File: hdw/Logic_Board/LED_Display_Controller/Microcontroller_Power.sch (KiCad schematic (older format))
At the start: 31 parts, among them U601 PIC32MZ2048EFH144_IPL

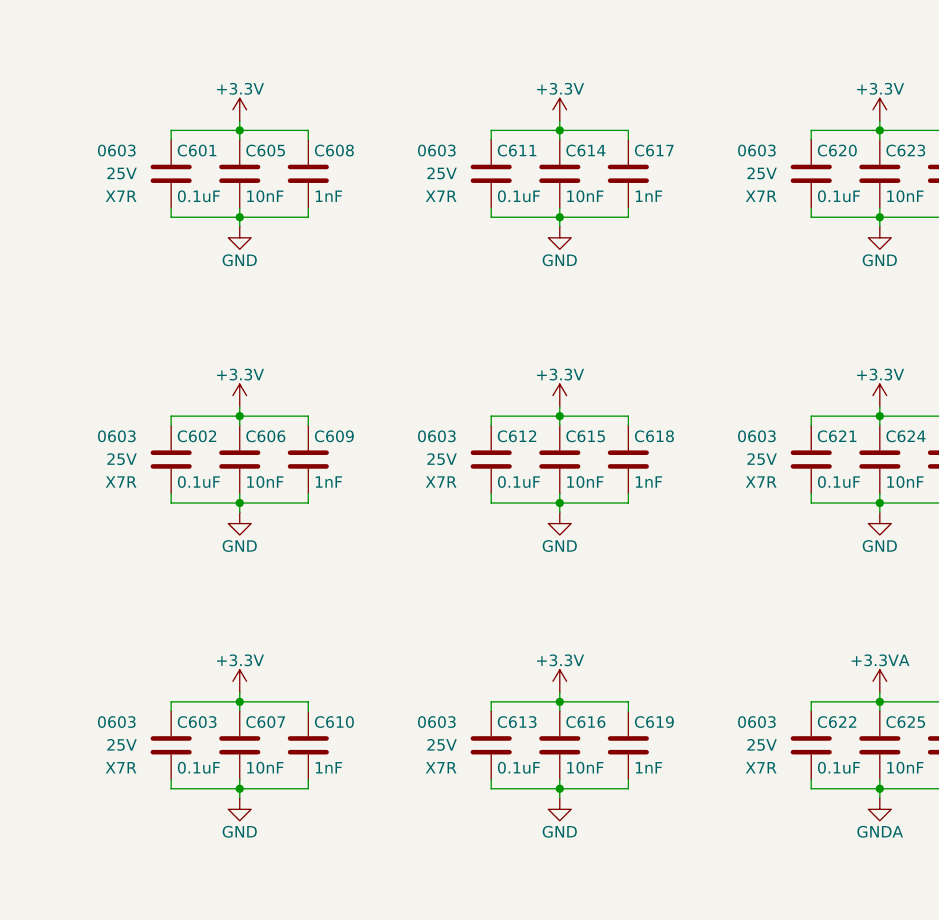
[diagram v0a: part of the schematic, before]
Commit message: Added some digikey partnumbers to components
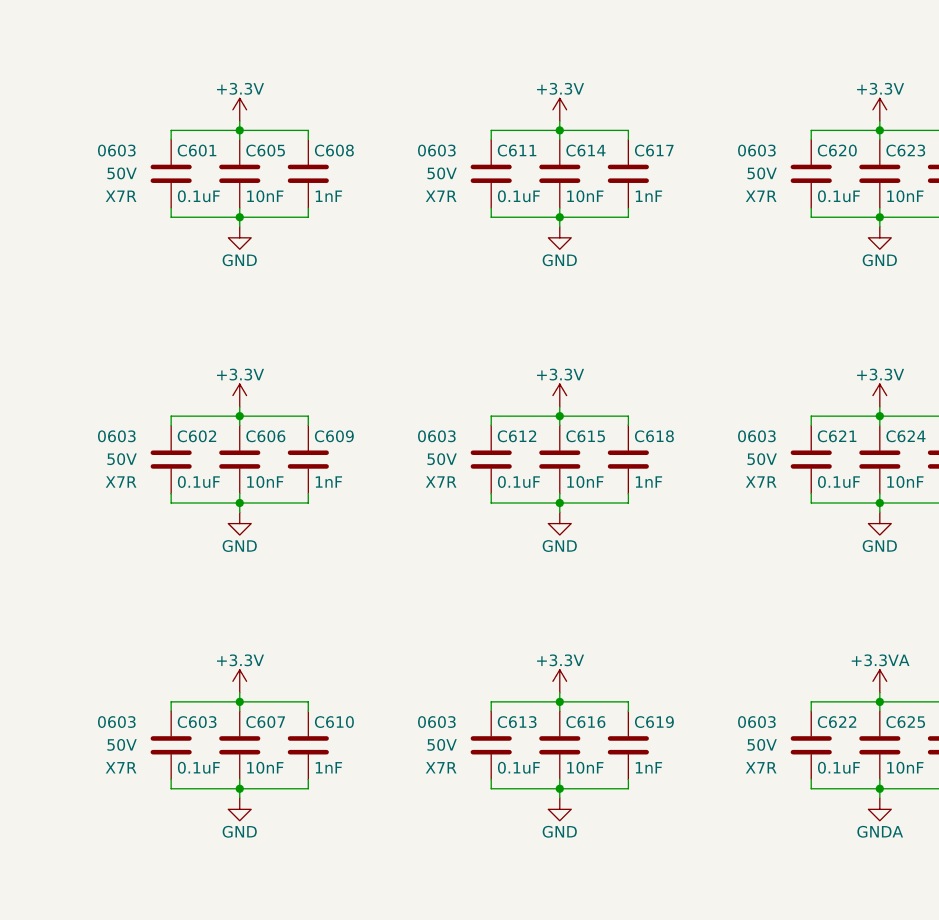
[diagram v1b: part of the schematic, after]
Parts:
- C601, C602, C603, C611, C612, C613, C620, C621, C622: footprint (none) -> Capacitors_SMD:C_0603; Digi-Key PN PN -> 311-1344-1-ND; Voltage 25V -> 50V
- C605, C606, C607, C614, C615, C616, C623, C624, C625: Digi-Key PN PN -> 1276-1921-1-ND; Voltage 25V -> 50V
- C608, C609, C610, C617, C618, C619, C626, C627, C628: Digi-Key PN PN -> 1276-1018-1-ND; Voltage 25V -> 50V
- L601, L602: Digi-Key PN (none) -> 732-2389-1-ND
- U601: Config ALL -> (none)

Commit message: First pass assignment of footprints to all components
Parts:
- C604: footprint (none) -> Capacitors_Tantalum_SMD:CP_Tantalum_Case-B_EIA-3528-21_Reflow
- C605, C606, C607, C608, C609, C610, C614, C615, C616, C617, C618, C619, C623, C624, C625, C626, C627, C628: footprint (none) -> Capacitors_SMD:C_0603
- L601, L602: footprint (none) -> Inductors_SMD:L_0603
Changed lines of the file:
@@
 F 0 "C605" H 1545 1750 50  0000 L CNN
 F 1 "10nF" H 1545 1550 50  0000 L CNN
-F 2 "" H 1558 1500 50  0001 C CNN
+F 2 "Capacitors_SMD:C_0603" H 1558 1500 50  0001 C CNN
 F 3 "" H 1545 1750 50  0001 C CNN
 F 4 "0603" H 1370 1750 50  0001 R CNN "display_footprint"
@@
 F 0 "C608" H 1845 1750 50  0000 L CNN
 F 1 "1nF" H 1845 1550 50  0000 L CNN
-F 2 "" H 1858 1500 50  0001 C CNN
+F 2 "Capacitors_SMD:C_0603" H 1858 1500 50  0001 C CNN
 F 3 "" H 1845 1750 50  0001 C CNN
 F 4 "0603" H 1670 1750 50  0001 R CNN "display_footprint"
@@
 F 0 "C614" H 2945 1750 50  0000 L CNN
 F 1 "10nF" H 2945 1550 50  0000 L CNN
-F 2 "" H 2958 1500 50  0001 C CNN
+F 2 "Capacitors_SMD:C_0603" H 2958 1500 50  0001 C CNN
 F 3 "" H 2945 1750 50  0001 C CNN
 F 4 "0603" H 2770 1750 50  0001 R CNN "display_footprint"
@@
 F 0 "C617" H 3245 1750 50  0000 L CNN
 F 1 "1nF" H 3245 1550 50  0000 L CNN
-F 2 "" H 3258 1500 50  0001 C CNN
+F 2 "Capacitors_SMD:C_0603" H 3258 1500 50  0001 C CNN
 F 3 "" H 3245 1750 50  0001 C CNN
 F 4 "0603" H 3070 1750 50  0001 R CNN "display_footprint"
@@
 F 0 "C623" H 4345 1750 50  0000 L CNN
 F 1 "10nF" H 4345 1550 50  0000 L CNN
-F 2 "" H 4358 1500 50  0001 C CNN
+F 2 "Capacitors_SMD:C_0603" H 4358 1500 50  0001 C CNN
 F 3 "" H 4345 1750 50  0001 C CNN
 F 4 "0603" H 4170 1750 50  0001 R CNN "display_footprint"
@@
 F 0 "C626" H 4645 1750 50  0000 L CNN
 F 1 "1nF" H 4645 1550 50  0000 L CNN
-F 2 "" H 4658 1500 50  0001 C CNN
+F 2 "Capacitors_SMD:C_0603" H 4658 1500 50  0001 C CNN
 F 3 "" H 4645 1750 50  0001 C CNN
 F 4 "0603" H 4470 1750 50  0001 R CNN "display_footprint"
@@
 F 0 "C606" H 1545 3000 50  0000 L CNN
 F 1 "10nF" H 1545 2800 50  0000 L CNN
-F 2 "" H 1558 2750 50  0001 C CNN
+F 2 "Capacitors_SMD:C_0603" H 1558 2750 50  0001 C CNN
 F 3 "" H 1545 3000 50  0001 C CNN
 F 4 "0603" H 1370 3000 50  0001 R CNN "display_footprint"
@@
 F 0 "C609" H 1845 3000 50  0000 L CNN
 F 1 "1nF" H 1845 2800 50  0000 L CNN
-F 2 "" H 1858 2750 50  0001 C CNN
+F 2 "Capacitors_SMD:C_0603" H 1858 2750 50  0001 C CNN
 F 3 "" H 1845 3000 50  0001 C CNN
 F 4 "0603" H 1670 3000 50  0001 R CNN "display_footprint"
@@
 F 0 "C615" H 2945 3000 50  0000 L CNN
 F 1 "10nF" H 2945 2800 50  0000 L CNN
-F 2 "" H 2958 2750 50  0001 C CNN
+F 2 "Capacitors_SMD:C_0603" H 2958 2750 50  0001 C CNN
 F 3 "" H 2945 3000 50  0001 C CNN
 F 4 "0603" H 2770 3000 50  0001 R CNN "display_footprint"
@@
 F 0 "C618" H 3245 3000 50  0000 L CNN
 F 1 "1nF" H 3245 2800 50  0000 L CNN
-F 2 "" H 3258 2750 50  0001 C CNN
+F 2 "Capacitors_SMD:C_0603" H 3258 2750 50  0001 C CNN
 F 3 "" H 3245 3000 50  0001 C CNN
 F 4 "0603" H 3070 3000 50  0001 R CNN "display_footprint"
@@
 F 0 "C624" H 4345 3000 50  0000 L CNN
 F 1 "10nF" H 4345 2800 50  0000 L CNN
-F 2 "" H 4358 2750 50  0001 C CNN
+F 2 "Capacitors_SMD:C_0603" H 4358 2750 50  0001 C CNN
 F 3 "" H 4345 3000 50  0001 C CNN
 F 4 "0603" H 4170 3000 50  0001 R CNN "display_footprint"
@@
 F 0 "C627" H 4645 3000 50  0000 L CNN
 F 1 "1nF" H 4645 2800 50  0000 L CNN
-F 2 "" H 4658 2750 50  0001 C CNN
+F 2 "Capacitors_SMD:C_0603" H 4658 2750 50  0001 C CNN
 F 3 "" H 4645 3000 50  0001 C CNN
 F 4 "0603" H 4470 3000 50  0001 R CNN "display_footprint"
@@
 F 0 "C607" H 1545 4250 50  0000 L CNN
 F 1 "10nF" H 1545 4050 50  0000 L CNN
-F 2 "" H 1558 4000 50  0001 C CNN
+F 2 "Capacitors_SMD:C_0603" H 1558 4000 50  0001 C CNN
 F 3 "" H 1545 4250 50  0001 C CNN
 F 4 "0603" H 1370 4250 50  0001 R CNN "display_footprint"
@@
 F 0 "C610" H 1845 4250 50  0000 L CNN
 F 1 "1nF" H 1845 4050 50  0000 L CNN
-F 2 "" H 1858 4000 50  0001 C CNN
+F 2 "Capacitors_SMD:C_0603" H 1858 4000 50  0001 C CNN
 F 3 "" H 1845 4250 50  0001 C CNN
 F 4 "0603" H 1670 4250 50  0001 R CNN "display_footprint"
@@
 F 0 "C616" H 2945 4250 50  0000 L CNN
 F 1 "10nF" H 2945 4050 50  0000 L CNN
-F 2 "" H 2958 4000 50  0001 C CNN
+F 2 "Capacitors_SMD:C_0603" H 2958 4000 50  0001 C CNN
 F 3 "" H 2945 4250 50  0001 C CNN
 F 4 "0603" H 2770 4250 50  0001 R CNN "display_footprint"
@@
 F 0 "C619" H 3245 4250 50  0000 L CNN
 F 1 "1nF" H 3245 4050 50  0000 L CNN
-F 2 "" H 3258 4000 50  0001 C CNN
+F 2 "Capacitors_SMD:C_0603" H 3258 4000 50  0001 C CNN
 F 3 "" H 3245 4250 50  0001 C CNN
 F 4 "0603" H 3070 4250 50  0001 R CNN "display_footprint"
@@
 F 0 "C625" H 4345 4250 50  0000 L CNN
 F 1 "10nF" H 4345 4050 50  0000 L CNN
-F 2 "" H 4358 4000 50  0001 C CNN
+F 2 "Capacitors_SMD:C_0603" H 4358 4000 50  0001 C CNN
 F 3 "" H 4345 4250 50  0001 C CNN
 F 4 "0603" H 4170 4250 50  0001 R CNN "display_footprint"
@@
 F 0 "C628" H 4645 4250 50  0000 L CNN
 F 1 "1nF" H 4645 4050 50  0000 L CNN
-F 2 "" H 4658 4000 50  0001 C CNN
+F 2 "Capacitors_SMD:C_0603" H 4658 4000 50  0001 C CNN
 F 3 "" H 4645 4250 50  0001 C CNN
 F 4 "0603" H 4470 4250 50  0001 R CNN "display_footprint"
@@
 F 0 "L601" V 2440 5815 50  0000 C CNN
 F 1 "600R 0.5A" V 2740 5790 50  0000 C CNN
-F 2 "" V 2520 5790 50  0001 C CNN
+F 2 "Inductors_SMD:L_0603" V 2520 5790 50  0001 C CNN
 F 3 "~" H 2590 5790 50  0001 C CNN
 F 4 "732-2389-1-ND" H 0   0   50  0001 C CNN "Digi-Key PN"
@@
 F 0 "L602" V 2440 6285 50  0000 C CNN
 F 1 "600R 0.5A" V 2740 6260 50  0000 C CNN
-F 2 "" V 2520 6260 50  0001 C CNN
+F 2 "Inductors_SMD:L_0603" V 2520 6260 50  0001 C CNN
 F 3 "~" H 2590 6260 50  0001 C CNN
 F 4 "732-2389-1-ND" H 0   0   50  0001 C CNN "Digi-Key PN"
@@
 F 0 "C604" H 1285 6080 50  0000 L CNN
 F 1 "100uF" H 1285 5880 50  0000 L CNN
-F 2 "" H 1298 5830 50  0001 C CNN
+F 2 "Capacitors_Tantalum_SMD:CP_Tantalum_Case-B_EIA-3528-21_Reflow" H 1298 5830 50  0001 C CNN
 F 3 "" H 1285 6080 50  0001 C CNN
 F 4 "399-5306-1-ND" H 1260 5980 50  0001 C CNN "Digi-Key PN"

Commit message: Modified BOM
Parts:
- C604: Digi-Key PN 399-5306-1-ND -> 478-3130-1-ND
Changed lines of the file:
@@
 F 2 "Capacitors_Tantalum_SMD:CP_Tantalum_Case-B_EIA-3528-21_Reflow" H 1298 5830 50  0001 C CNN
 F 3 "" H 1285 6080 50  0001 C CNN
-F 4 "399-5306-1-ND" H 1260 5980 50  0001 C CNN "Digi-Key PN"
+F 4 "478-3130-1-ND" H 1260 5980 50  0001 C CNN "Digi-Key PN"
 F 5 "3528" H 1110 6080 50  0000 R CNN "display_footprint"
 F 6 "6.3V" H 1110 5980 50  0000 R CNN "Voltage"
